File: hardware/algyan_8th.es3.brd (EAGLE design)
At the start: 142 x 55 mm, 43 parts, among them CN1 4P-2.0, U1 XIAO ESP32C3, U10 EC12E(Panel), U2 TM1640, U3 NJM2113M, U4 LTP-12188M-08, U5 NJM2113D, U6 UGSM23A, U7 EC12PLRVF, U8 TVGP01-G73BB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

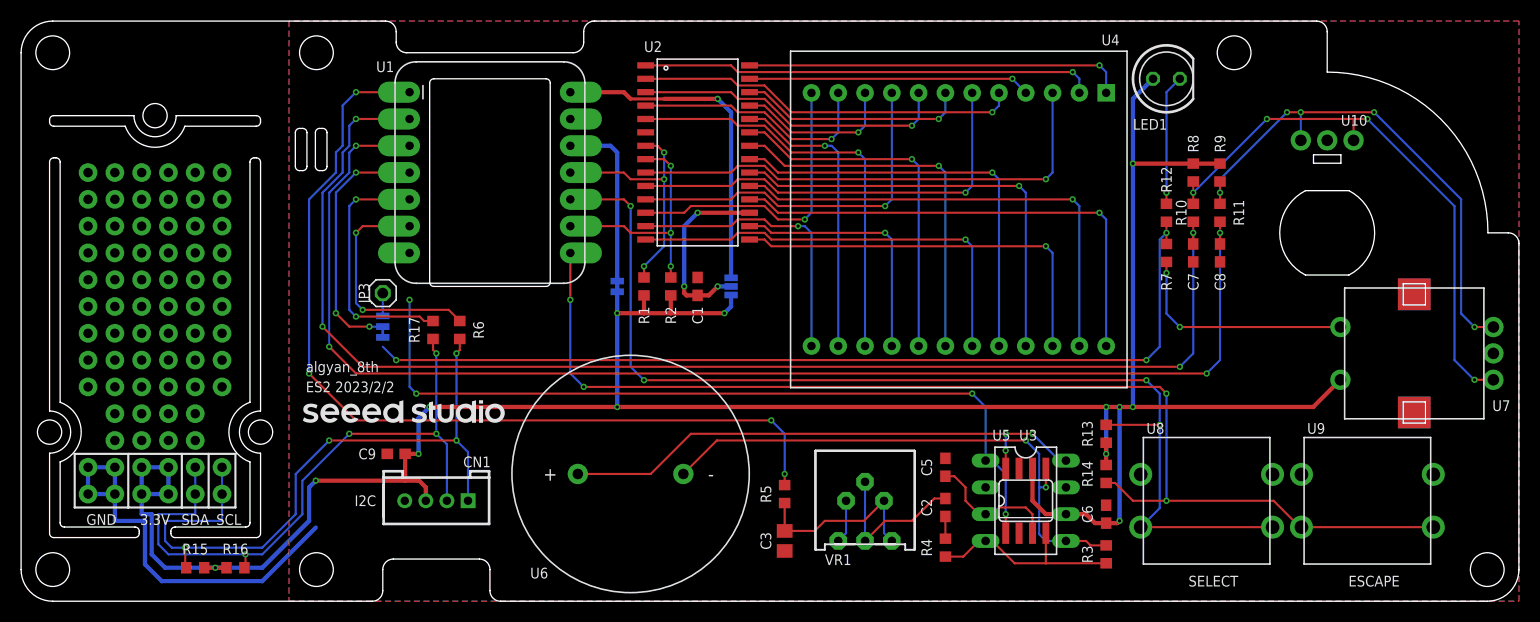
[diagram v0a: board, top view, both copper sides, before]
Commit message: ES3基板のEAGLEファイルと回路図PDFを追加
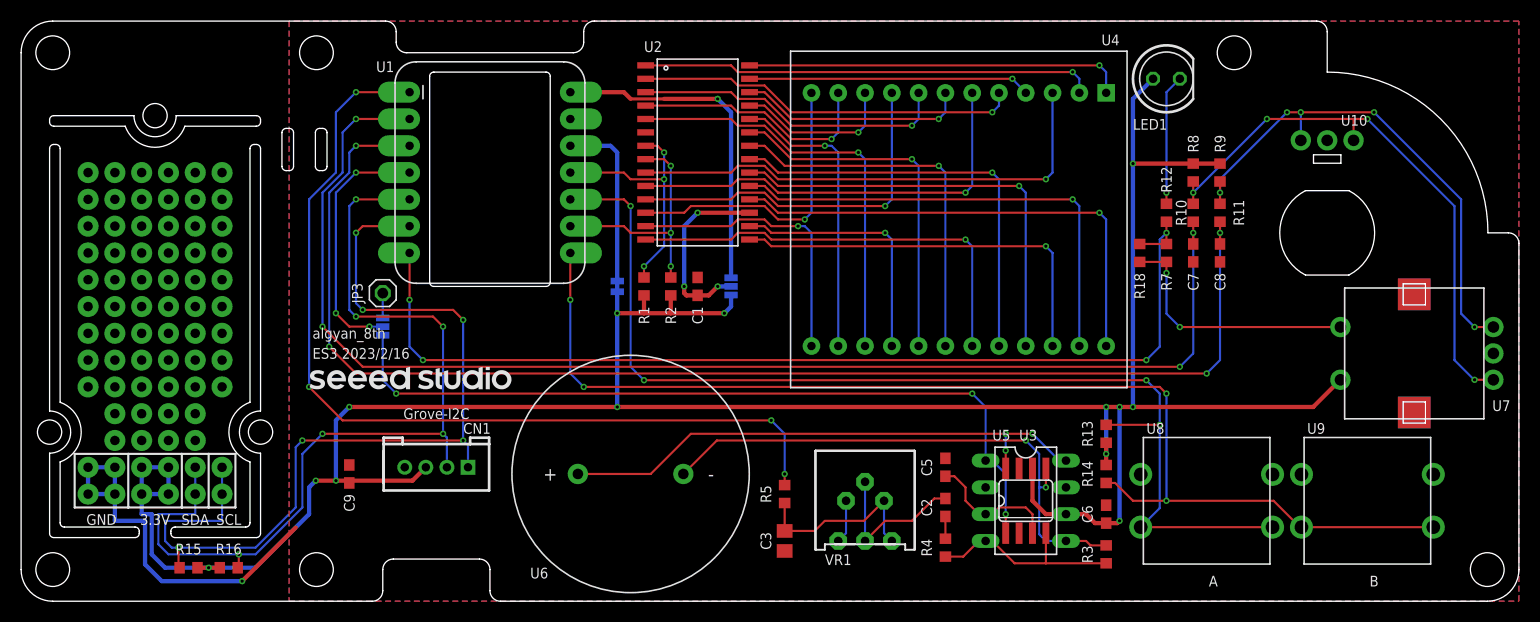
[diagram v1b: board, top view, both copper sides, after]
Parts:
- removed R17, R6: 0, rcl:R0603
- added R18: 10K, rcl:R0603
- JP2: value JUMPER-SMT_3_1-NC_TRACE_SILK -> JUMPER-SMT_3_NO_SILK; device SparkFun-Jumpers:SMT-JUMPER_3_1-NC_TRACE_SILK -> SparkFun-Jumpers:SMT-JUMPER_3_NO_SILK
- R1, R2: value 100K -> 10K
- R7: value (none) -> 10K
- moved C9 4.84 mm to (31.1, 12.1), turned to 90 degrees
- moved CN1 3.17 mm to (39.4, 12.7)
- moved R15 0.64 mm to (15.9, 3.17)
- moved R16 0.64 mm to (19.7, 3.17)
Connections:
- removed net N$17: CN1.1, R15.1, R6.1
- removed net N$18: CN1.2, R16.1, R17.1
- net LED: now also R18.1
- net N$6: now also R18.2
- net SCL: now also CN1.1, R15.1; no longer R6.2
- net SDA: now also CN1.2, R16.1; no longer R17.2
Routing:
- net SCL: track 22.6 -> 87.5 mm, vias 2 -> 8
- net N$17: track 64.6 -> 0.00 mm, vias 6 -> 0
- net SDA: track 24.2 -> 86.1 mm, vias 2 -> 8
- net N$18: track 61.4 -> 0.00 mm, vias 6 -> 0
- net LED: track 87.9 -> 96.8 mm, vias 3 -> 4
- net 3V3: track 244.6 -> 249.9 mm
- net N$6: track 21.9 -> 24.5 mm
- net GND: track 42.8 -> 40.9 mm, vias 4 -> 5
- net SPEAKER-ENABLE: track 76.8 -> 75.6 mm, vias 4 -> 3
- net SPEAKER: track 85.9 -> 86.7 mm
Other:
- outline, holes or cut-outs redrawn
- board text added: "3V3"
- board text added: "5V"
- board text added: "A"
- board text added: "A-BTN"
- board text added: "AIN"
- board text added: "B"
- board text added: "B-BTN"
- board text added: "DIN"
- board text added: "ENCA"
- board text added: "ENCB"
- board text added: "ES3 2023/2/16"
- board text added: "Grove-I2C"
- board text added: "LED"
- board text added: "SCLK"
- board text added: "SP"
- board text added: "SPEN"
- board text added: "SPEN /AIN"
- board text removed: "ES2 2023/2/2"
- board text removed: "ESCAPE"
- board text removed: "I2C"
- board text removed: "SELECT"
